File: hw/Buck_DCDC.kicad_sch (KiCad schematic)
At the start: 6 parts, among them U4 AP3410K

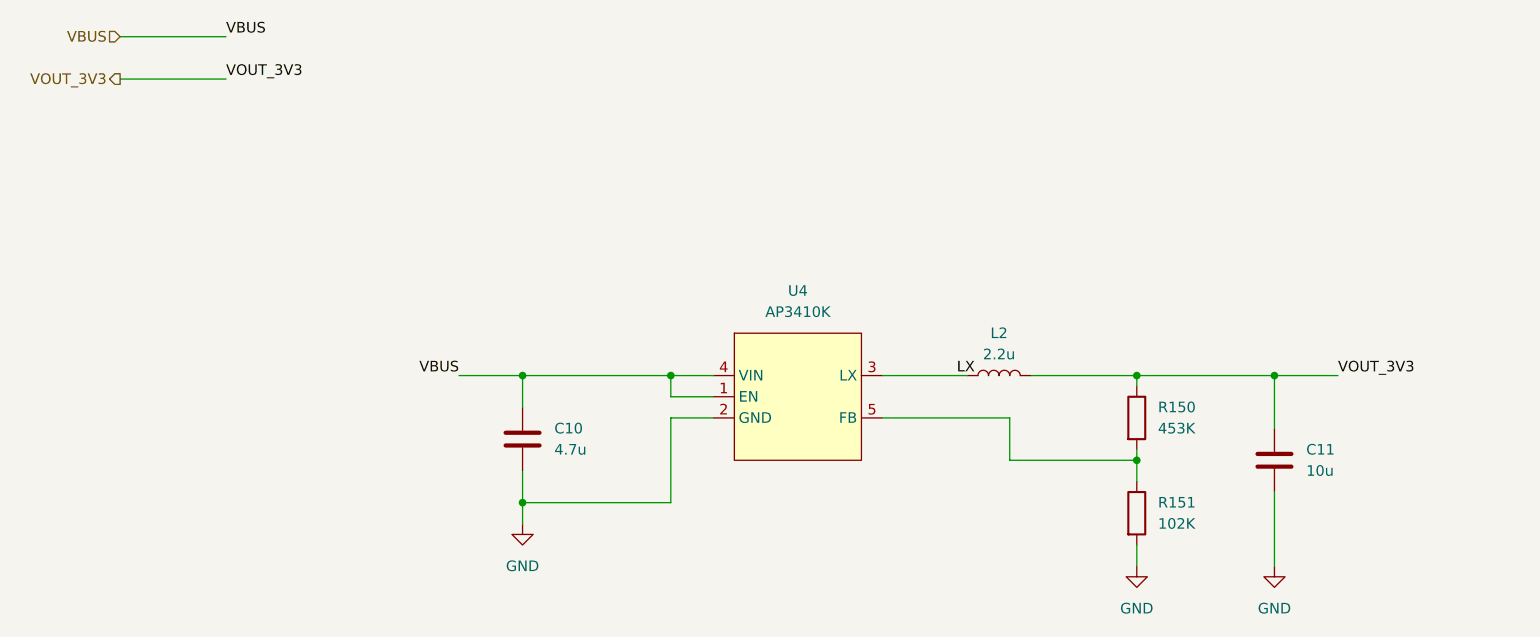
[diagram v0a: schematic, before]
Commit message: replace AP3410 to SY8088IAAC
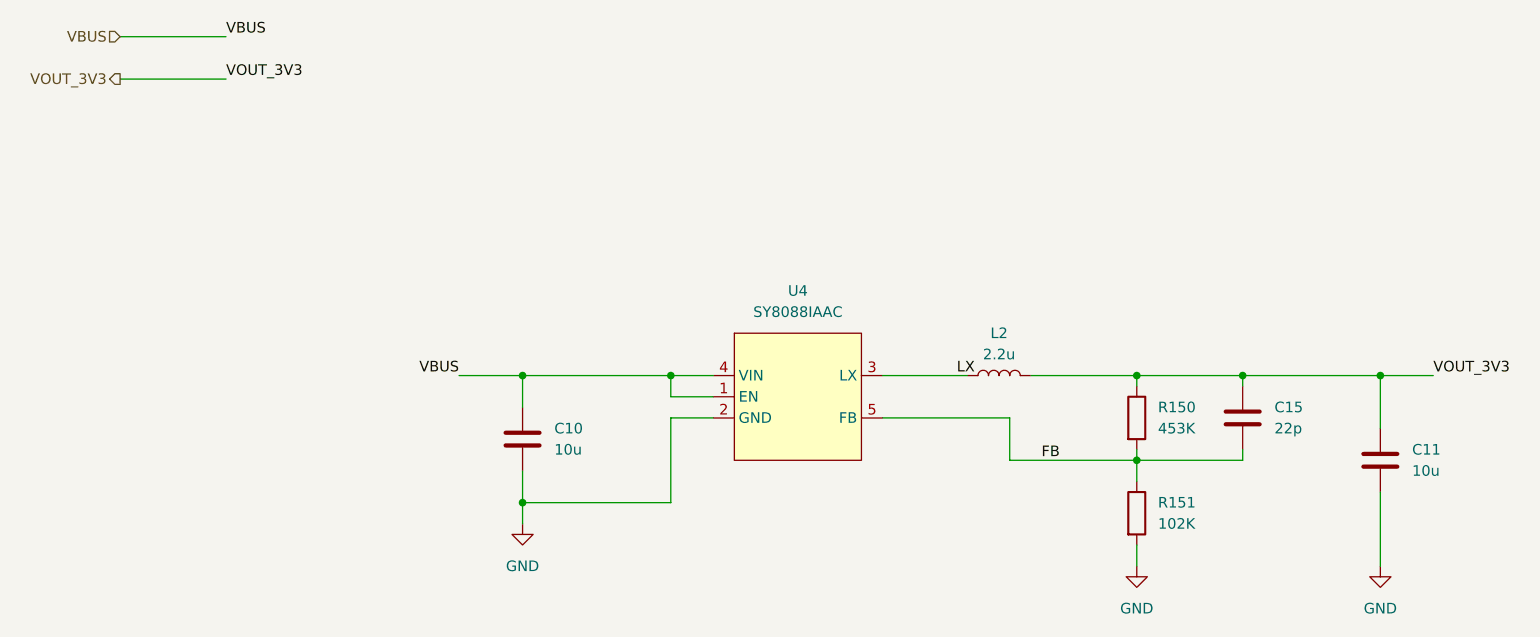
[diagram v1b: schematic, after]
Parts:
- removed U4: AP3410K, Package_TO_SOT_SMD:SOT-23-5_HandSoldering, symbol IotPi_Regulator_Switching:AP3410K
- added C15: 22p, Capacitor_SMD:C_0805_2012Metric, symbol Device:C
- added U4: SY8088IAAC, Package_TO_SOT_SMD:SOT-23-5, symbol IotPi_Regulator_Switching:SY8088IAAC
- C10: value 4.7u -> 10u; LCSC C1779 -> C15850; Vendor Model CL21A475KAQNNNE -> CL21A106KAYNNNE
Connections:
- net GND: now also U4.2 (GND)
- net LX: now also U4.3 (LX)
- net VBUS: now also U4.1 (EN), U4.4 (VIN)
- net VOUT_3V3: now also C15.1
- net FB: now reaches R150.2, R151.1
- net FB: now also C15.2, U4.5 (FB)
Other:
- moved on the sheet: C11

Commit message: updated Sheet and Board Information
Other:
- company: Qingdao IotPi Information Technology Ltd., -> Beijing Exponential Deep Space
- title: KiCad 2023 Shen Zhen Badge -> KiCad 2023 Asia Badge
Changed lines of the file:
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@@
   (paper "A4")
   (title_block
-    (title "KiCad 2023 Shen Zhen Badge")
-    (date "2023-10-04")
+    (title "KiCad 2023 Asia Badge")
+    (date "2023-10-07")
     (rev "2")
-    (company "Qingdao IotPi Information Technology Ltd.,")
+    (company "Beijing Exponential Deep Space")
     (comment 1 "Designed by Yang Hongbo")
   )
